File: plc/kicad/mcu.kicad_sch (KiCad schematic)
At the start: 57 parts, among them J2 Conn_01x04_Pin, Q3 L8050QLT1G, Q4 L8050QLT1G, SW1 TSD003B08026A03, SW2 TSD003B08026A03, U10 ESP32-S3-MINI-1U, U11 BS-0601-SK-4W, U12 AHT20_C2757850, U13 CP2102N-A02-GQFN28R, U9 RV-3028-C7

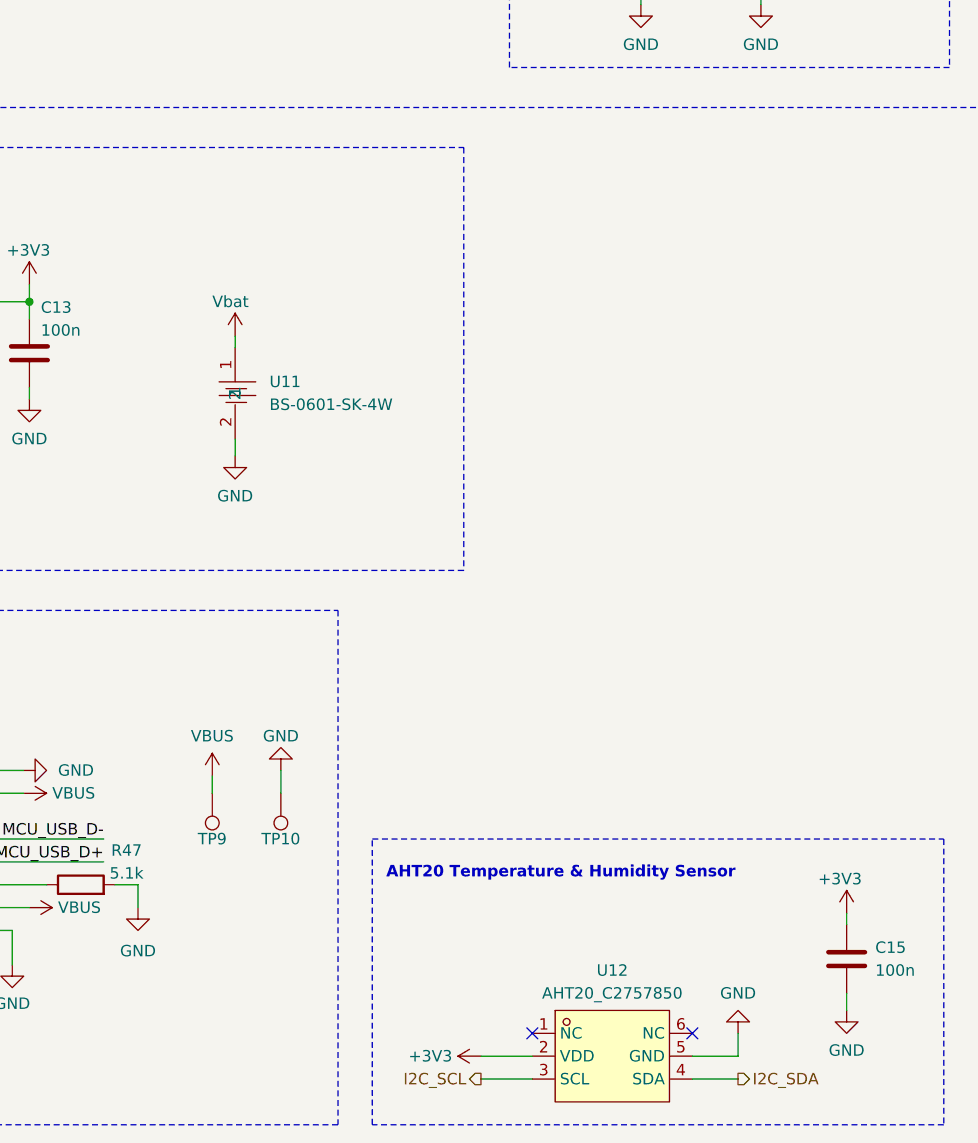
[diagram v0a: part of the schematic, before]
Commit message: Added i2c addresses & TPS26630 modifications
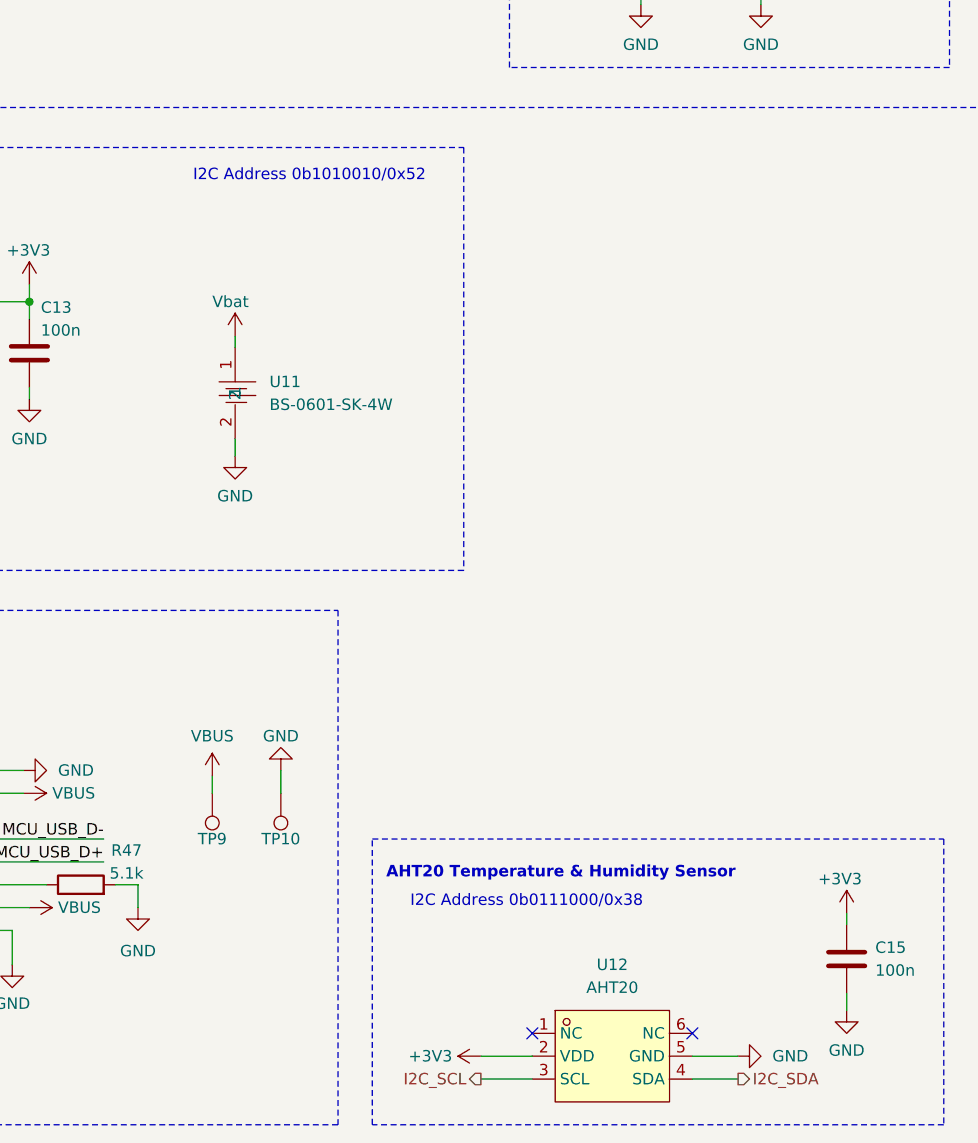
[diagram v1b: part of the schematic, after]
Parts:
- U12: value AHT20_C2757850 -> AHT20
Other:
- note added: "I2C Address 0b0111000/0x38"
- note added: "I2C Address 0b1010010/0x52"
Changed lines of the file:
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@@
 		)
 	)
+	(text "I2C Address 0b1010010/0x52\n"
+		(exclude_from_sim no)
+		(at 122.555 172.72 0)
+		(effects
+			(font
+				(size 1.27 1.27)
+			)
+		)
+	)
 	(text "Status LEDs"
 		(exclude_from_sim no)
@@
 		)
 	)
+	(text "I2C Address 0b0111000/0x38\n"
+		(exclude_from_sim no)
+		(at 146.685 253.365 0)
+		(effects
+			(font
+				(size 1.27 1.27)
+			)
+		)
+	)
 	(text "Boot Circuit"
 		(exclude_from_sim no)
@@
 		)
 	)
-	(wire
-		(pts
-			(xy 170.18 267.97) (xy 170.18 270.51)
-		)
-		(stroke
-			(width 0)
-			(type default)
-		)
-	)
 	(bus
 		(pts
@@
 	(symbol
 		(lib_id "power:GND")
-		(at 170.18 267.97 180)
+		(at 170.18 270.51 90)
 		(unit 1)
 		(body_style 1)
@@
 		(fields_autoplaced yes)
 		(property "Reference" "#PWR099"
-			(at 170.18 261.62 0)
+			(at 176.53 270.51 0)
 			(hide yes)
 			(show_name no)
@@
 		)
 		(property "Value" "GND"
-			(at 170.18 263.525 0)
+			(at 173.99 270.5099 90)
 			(show_name no)
 			(do_not_autoplace no)
@@
 					(size 1.27 1.27)
 				)
+				(justify right)
 			)
 		)
 		(property "Footprint" ""
-			(at 170.18 267.97 0)
+			(at 170.18 270.51 0)
 			(hide yes)
 			(show_name no)
@@
 		)
 		(property "Datasheet" ""
-			(at 170.18 267.97 0)
+			(at 170.18 270.51 0)
 			(hide yes)
 			(show_name no)
@@
 		)
 		(property "Description" "Power symbol creates a global label with name \"GND\" , ground"
-			(at 170.18 267.97 0)
+			(at 170.18 270.51 0)
 			(hide yes)
 			(show_name no)
@@
 		(fields_autoplaced yes)
 		(property "Reference" "U12"
-			(at 156.21 260.985 0)
+			(at 156.21 260.35 0)
 			(show_name no)
 			(do_not_autoplace no)
@@
 			)
 		)
-		(property "Value" "AHT20_C2757850"
-			(at 156.21 263.525 0)
+		(property "Value" "AHT20"
+			(at 156.21 262.89 0)
 			(show_name no)
 			(do_not_autoplace no)

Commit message: Needed fixes
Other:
- note added: "ADD MCU RST"
- note added: "SWITCH RX AND TX FOR UART"
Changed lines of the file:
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@@
 		)
 	)
+	(text "SWITCH RX AND TX FOR UART"
+		(exclude_from_sim no)
+		(at 316.484 55.88 0)
+		(effects
+			(font
+				(size 3 3)
+				(thickness 0.6)
+				(bold yes)
+			)
+		)
+	)
+	(text "ADD MCU RST"
+		(exclude_from_sim no)
+		(at 75.565 47.625 0)
+		(effects
+			(font
+				(size 3 3)
+				(thickness 0.6)
+				(bold yes)
+			)
+		)
+	)
 	(text "I2C Address 0b0111000/0x38\n"
 		(exclude_from_sim no)
@@
 	)
 	(junction
-		(at 251.714 61.214)
+		(at 251.46 61.214)
 		(diameter 0)
 		(color 0 0 0 0)
@@
 	(wire
 		(pts
-			(xy 251.714 61.214) (xy 251.714 63.119)
+			(xy 251.46 61.214) (xy 251.46 62.865)
 		)
 		(stroke
@@
 	(wire
 		(pts
-			(xy 251.714 60.579) (xy 251.714 61.214)
+			(xy 251.46 59.69) (xy 251.46 61.214)
 		)
 		(stroke
@@
 	(wire
 		(pts
-			(xy 251.714 73.279) (xy 251.714 70.739)
+			(xy 251.46 73.025) (xy 251.46 70.485)
 		)
 		(stroke
@@
 	(wire
 		(pts
-			(xy 251.714 61.214) (xy 277.114 61.214)
-		)
-		(stroke
-			(width 0)
-			(type default)
-		)
-	)
-	(wire
-		(pts
 			(xy 170.18 273.05) (xy 165.1 273.05)
 		)
@@
 	(wire
 		(pts
+			(xy 251.46 61.214) (xy 277.114 61.214)
+		)
+		(stroke
+			(width 0)
+			(type default)
+		)
+	)
+	(wire
+		(pts
 			(xy 376.555 179.705) (xy 376.555 182.245)
 		)
@@
 	(symbol
 		(lib_id "power:+3V3")
-		(at 251.714 60.579 0)
+		(at 251.46 59.69 0)
 		(unit 1)
 		(body_style 1)
@@
 		(fields_autoplaced yes)
 		(property "Reference" "#PWR0109"
-			(at 251.714 64.389 0)
+			(at 251.46 63.5 0)
 			(hide yes)
 			(show_name no)
@@
 		)
 		(property "Value" "+3V3"
-			(at 251.714 55.499 0)
+			(at 251.46 54.61 0)
 			(show_name no)
 			(do_not_autoplace no)
@@
 		)
 		(property "Footprint" ""
-			(at 251.714 60.579 0)
+			(at 251.46 59.69 0)
 			(hide yes)
 			(show_name no)
@@
 		)
 		(property "Datasheet" ""
-			(at 251.714 60.579 0)
+			(at 251.46 59.69 0)
 			(hide yes)
 			(show_name no)
@@
 		)
 		(property "Description" "Power symbol creates a global label with name \"+3V3\""
-			(at 251.714 60.579 0)
+			(at 251.46 59.69 0)
 			(hide yes)
 			(show_name no)
@@
 	(symbol
 		(lib_id "power:GND")
-		(at 251.714 73.279 0)
+		(at 251.46 73.025 0)
 		(unit 1)
 		(body_style 1)
@@
 		(dnp no)
 		(property "Reference" "#PWR0110"
-			(at 251.714 79.629 0)
+			(at 251.46 79.375 0)
 			(hide yes)
 			(show_name no)
@@
 		)
 		(property "Value" "GND"
-			(at 251.714 77.724 0)
+			(at 251.46 77.47 0)
 			(show_name no)
 			(do_not_autoplace no)
@@
 		)
 		(property "Footprint" ""
-			(at 251.714 73.279 0)
+			(at 251.46 73.025 0)
 			(hide yes)
 			(show_name no)
@@
 		)
 		(property "Datasheet" ""
-			(at 251.714 73.279 0)
+			(at 251.46 73.025 0)
 			(hide yes)
 			(show_name no)
@@
 		)
 		(property "Description" "Power symbol creates a global label with name \"GND\" , ground"
-			(at 251.714 73.279 0)
+			(at 251.46 73.025 0)
 			(hide yes)
 			(show_name no)
@@
 	(symbol
 		(lib_id "Device:C")
-		(at 251.714 66.929 180)
+		(at 251.46 66.675 180)
 		(unit 1)
 		(body_style 1)
@@
 		(dnp no)
 		(property "Reference" "C16"
-			(at 244.729 66.294 0)
+			(at 244.475 66.04 0)
 			(show_name no)
 			(do_not_autoplace no)
@@
 		)
 		(property "Value" "10u"
-			(at 244.729 68.834 0)
+			(at 244.475 68.58 0)
 			(show_name no)
 			(do_not_autoplace no)
@@
 		)
 		(property "Footprint" "Capacitor_SMD:C_0603_1608Metric"
-			(at 250.7488 63.119 0)
+			(at 250.4948 62.865 0)
 			(hide yes)
 			(show_name no)
@@
 		)
 		(property "Datasheet" ""
-			(at 251.714 66.929 0)
+			(at 251.46 66.675 0)
 			(hide yes)
 			(show_name no)
@@
 		)
 		(property "Description" "Unpolarized capacitor"
-			(at 251.714 66.929 0)
+			(at 251.46 66.675 0)
 			(hide yes)
 			(show_name no)
